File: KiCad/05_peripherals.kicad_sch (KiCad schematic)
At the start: 37 parts, among them IC501 VEML7700-TT, IC502 DS3231MZ+TRL, U502 DS18B20, U503 LM35-LP, U504 DHT11

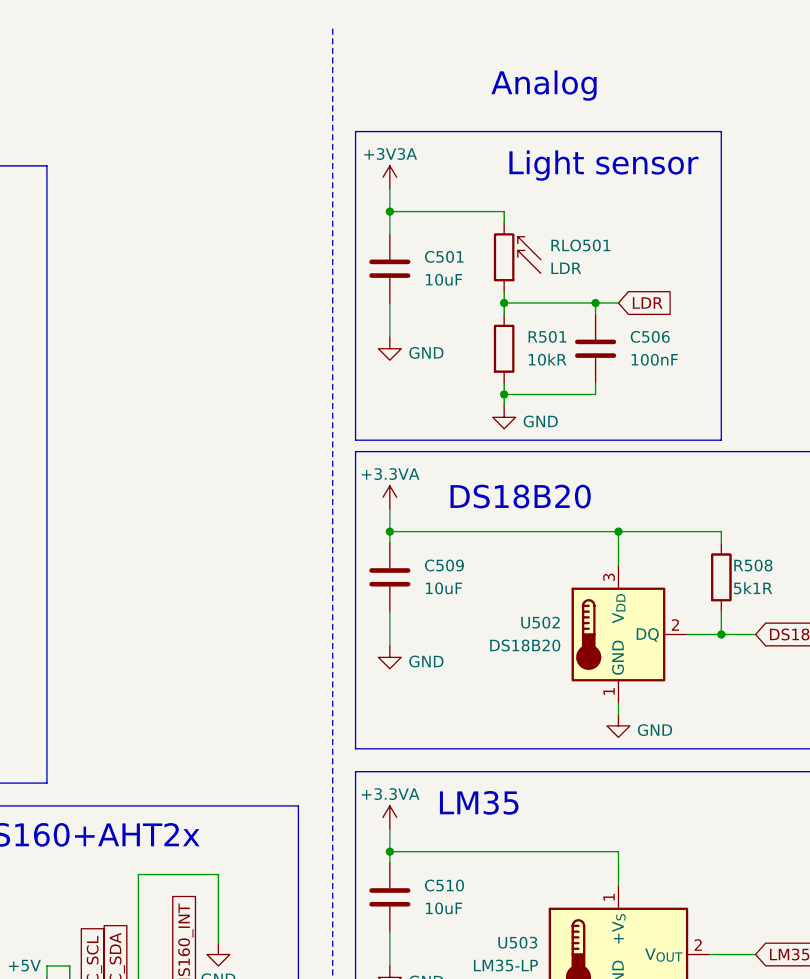
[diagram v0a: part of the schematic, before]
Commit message: Remove 3V3A power chain
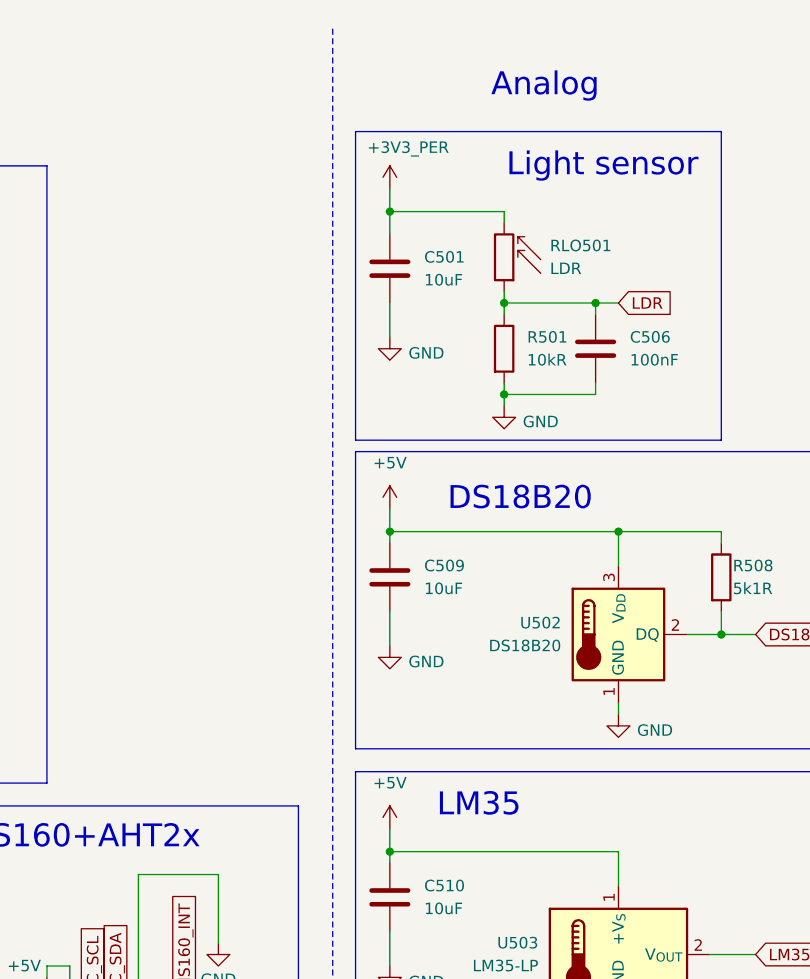
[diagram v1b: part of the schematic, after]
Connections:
- net +3.3VA is gone; now on net +5V: C509.1, C510.1, R508.1, U502.3 (V_{DD}), U503.1 (+V_{S})
- net +3V3A is gone; now on net +3V3_PER: C501.1, RLO501.2
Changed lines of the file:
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@@
 	)
 	(symbol
-		(lib_name "+3.3VA_1")
-		(lib_id "power:+3.3VA")
-		(at 224.79 104.14 0)
-		(unit 1)
-		(exclude_from_sim no)
-		(in_bom yes)
-		(on_board yes)
-		(dnp no)
-		(property "Reference" "#PWR0519"
-			(at 224.79 107.95 0)
-			(effects
-				(font
-					(size 1.27 1.27)
-				)
-				(hide yes)
-			)
-		)
-		(property "Value" "+3.3VA"
-			(at 224.79 100.33 0)
-			(effects
-				(font
-					(size 1.27 1.27)
-				)
-			)
-		)
-		(property "Footprint" ""
-			(at 224.79 104.14 0)
-			(effects
-				(font
-					(size 1.27 1.27)
-				)
-				(hide yes)
-			)
-		)
-		(property "Datasheet" ""
-			(at 224.79 104.14 0)
-			(effects
-				(font
-					(size 1.27 1.27)
-				)
-				(hide yes)
-			)
-		)
-		(property "Description" "Power symbol creates a global label with name \"+3.3VA\""
-			(at 224.79 104.14 0)
-			(effects
-				(font
-					(size 1.27 1.27)
-				)
-				(hide yes)
-			)
-		)
-		(pin "1"
-		)
-		(instances
-			(project "esp32_s3_weather_webserver"
-				(path "/04e96486-ec4c-4881-a0bf-37cb6ce91c2d/c3c48617-55df-481a-bcdd-56b688125780"
-					(reference "#PWR0519")
-					(unit 1)
-				)
-			)
-		)
-	)
-	(symbol
 		(lib_id "Device:C")
 		(at 62.23 116.84 0)
@@
 	)
 	(symbol
-		(lib_id "power:+3.3VA")
-		(at 224.79 33.02 0)
-		(unit 1)
-		(exclude_from_sim no)
-		(in_bom yes)
-		(on_board yes)
-		(dnp no)
-		(property "Reference" "#PWR0501"
-			(at 224.79 36.83 0)
-			(effects
-				(font
-					(size 1.27 1.27)
-				)
-				(hide yes)
-			)
-		)
-		(property "Value" "+3V3A"
-			(at 224.79 29.21 0)
-			(effects
-				(font
-					(size 1.27 1.27)
-				)
-			)
-		)
-		(property "Footprint" ""
-			(at 224.79 33.02 0)
-			(effects
-				(font
-					(size 1.27 1.27)
-				)
-				(hide yes)
-			)
-		)
-		(property "Datasheet" ""
-			(at 224.79 33.02 0)
-			(effects
-				(font
-					(size 1.27 1.27)
-				)
-				(hide yes)
-			)
-		)
-		(property "Description" "Power symbol creates a global label with name \"+3.3VA\""
-			(at 224.79 33.02 0)
-			(effects
-				(font
-					(size 1.27 1.27)
-				)
-				(hide yes)
-			)
-		)
-		(pin "1"
-		)
-		(instances
-			(project "esp32_s3_weather_webserver"
-				(path "/04e96486-ec4c-4881-a0bf-37cb6ce91c2d/c3c48617-55df-481a-bcdd-56b688125780"
-					(reference "#PWR0501")
-					(unit 1)
-				)
-			)
-		)
-	)
-	(symbol
 		(lib_id "esp32_s3_weather_webserver:SW_PUSH_6mm_H5mm")
 		(at 106.68 175.26 0)
@@
 	)
 	(symbol
+		(lib_id "power:+5V")
+		(at 224.79 104.14 0)
+		(mirror y)
+		(unit 1)
+		(exclude_from_sim no)
+		(in_bom yes)
+		(on_board yes)
+		(dnp no)
+		(fields_autoplaced yes)
+		(property "Reference" "#PWR014"
+			(at 224.79 107.95 0)
+			(effects
+				(font
+					(size 1.27 1.27)
+				)
+				(hide yes)
+			)
+		)
+		(property "Value" "+5V"
+			(at 224.79 99.06 0)
+			(effects
+				(font
+					(size 1.27 1.27)
+				)
+			)
+		)
+		(property "Footprint" ""
+			(at 224.79 104.14 0)
+			(effects
+				(font
+					(size 1.27 1.27)
+				)
+				(hide yes)
+			)
+		)
+		(property "Datasheet" ""
+			(at 224.79 104.14 0)
+			(effects
+				(font
+					(size 1.27 1.27)
+				)
+				(hide yes)
+			)
+		)
+		(property "Description" "Power symbol creates a global label with name \"+5V\""
+			(at 224.79 104.14 0)
+			(effects
+				(font
+					(size 1.27 1.27)
+				)
+				(hide yes)
+			)
+		)
+		(pin "1"
+		)
+		(instances
+			(project "esp32_s3_weather_webserver"
+				(path "/04e96486-ec4c-4881-a0bf-37cb6ce91c2d/c3c48617-55df-481a-bcdd-56b688125780"
+					(reference "#PWR014")
+					(unit 1)
+				)
+			)
+		)
+	)
+	(symbol
 		(lib_id "Device:C")
 		(at 134.62 119.38 0)
@@
 	)
 	(symbol
+		(lib_id "power:+5V")
+		(at 224.79 68.58 0)
+		(mirror y)
+		(unit 1)
+		(exclude_from_sim no)
+		(in_bom yes)
+		(on_board yes)
+		(dnp no)
+		(fields_autoplaced yes)
+		(property "Reference" "#PWR015"
+			(at 224.79 72.39 0)
+			(effects
+				(font
+					(size 1.27 1.27)
+				)
+				(hide yes)
+			)
+		)
+		(property "Value" "+5V"
+			(at 224.79 63.5 0)
+			(effects
+				(font
+					(size 1.27 1.27)
+				)
+			)
+		)
+		(property "Footprint" ""
+			(at 224.79 68.58 0)
+			(effects
+				(font
+					(size 1.27 1.27)
+				)
+				(hide yes)
+			)
+		)
+		(property "Datasheet" ""
+			(at 224.79 68.58 0)
+			(effects
+				(font
+					(size 1.27 1.27)
+				)
+				(hide yes)
+			)
+		)
+		(property "Description" "Power symbol creates a global label with name \"+5V\""
+			(at 224.79 68.58 0)
+			(effects
+				(font
+					(size 1.27 1.27)
+				)
+				(hide yes)
+			)
+		)
+		(pin "1"
+		)
+		(instances
+			(project "esp32_s3_weather_webserver"
+				(path "/04e96486-ec4c-4881-a0bf-37cb6ce91c2d/c3c48617-55df-481a-bcdd-56b688125780"
+					(reference "#PWR015")
+					(unit 1)
+				)
+			)
+		)
+	)
+	(symbol
 		(lib_id "power:+3.3V")
 		(at 123.19 113.03 0)
@@
 	)
 	(symbol
-		(lib_name "+3.3VA_2")
-		(lib_id "power:+3.3VA")
-		(at 224.79 68.58 0)
-		(unit 1)
-		(exclude_from_sim no)
-		(in_bom yes)
-		(on_board yes)
-		(dnp no)
-		(property "Reference" "#PWR0512"
-			(at 224.79 72.39 0)
-			(effects
-				(font
-					(size 1.27 1.27)
-				)
-				(hide yes)
-			)
-		)
-		(property "Value" "+3.3VA"
-			(at 224.79 64.77 0)
-			(effects
-				(font
-					(size 1.27 1.27)
-				)
-			)
-		)
-		(property "Footprint" ""
-			(at 224.79 68.58 0)
-			(effects
-				(font
-					(size 1.27 1.27)
-				)
-				(hide yes)
-			)
-		)
-		(property "Datasheet" ""
-			(at 224.79 68.58 0)
-			(effects
-				(font
-					(size 1.27 1.27)
-				)
-				(hide yes)
-			)
-		)
-		(property "Description" "Power symbol creates a global label with name \"+3.3VA\""
-			(at 224.79 68.58 0)
-			(effects
-				(font
-					(size 1.27 1.27)
-				)
-				(hide yes)
-			)
-		)
-		(pin "1"
-		)
-		(instances
-			(project "esp32_s3_weather_webserver"
-				(path "/04e96486-ec4c-4881-a0bf-37cb6ce91c2d/c3c48617-55df-481a-bcdd-56b688125780"
-					(reference "#PWR0512")
-					(unit 1)
-				)
-			)
-		)
-	)
-	(symbol
 		(lib_id "Device:C")
 		(at 50.8 116.84 0)
@@
 					(unit 1)
 				)
+			)
+		)
+	)
+	(symbol
+		(lib_id "power:+3.3V")
+		(at 224.79 33.02 0)
+		(unit 1)
+		(exclude_from_sim no)
+		(in_bom yes)
+		(on_board yes)
+		(dnp no)
+		(property "Reference" "#PWR016"
+			(at 224.79 36.83 0)
+			(effects
+				(font
+					(size 1.27 1.27)
+				)
+				(hide yes)
+			)
+		)
+		(property "Value" "+3V3_PER"
+			(at 226.822 28.448 0)
+			(effects
+				(font
+					(size 1.27 1.27)
+				)
+			)
+		)
+		(property "Footprint" ""
+			(at 224.79 33.02 0)
+			(effects
+				(font
+					(size 1.27 1.27)
+				)
+				(hide yes)
+			)
+		)
+		(property "Datasheet" ""
+			(at 224.79 33.02 0)
+			(effects
+				(font
+					(size 1.27 1.27)
+				)
+				(hide yes)
+			)
+		)
+		(property "Description" "Power symbol creates a global label with name \"+3.3V\""
+			(at 224.79 33.02 0)
+			(effects
+				(font
+					(size 1.27 1.27)
+				)
+				(hide yes)
+			)
+		)
+		(pin "1"
+		)
+		(instances
+			(project "esp32_s3_weather_webserver"
+				(path "/04e96486-ec4c-4881-a0bf-37cb6ce91c2d/c3c48617-55df-481a-bcdd-56b688125780"
+					(reference "#PWR016")
+					(unit 1)
+				)

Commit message: Add sensor footprints
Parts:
- U1: footprint (none) -> esp32_s3_weather_webserver:BME280
- U505: footprint (none) -> esp32_s3_weather_webserver:ENS160+AHT2x
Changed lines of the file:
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@@
 			)
 		)
-		(property "Footprint" ""
+		(property "Footprint" "esp32_s3_weather_webserver:ENS160+AHT2x"
 			(at 182.88 129.54 0)
 			(effects
@@
 			)
 		)
-		(property "Footprint" ""
+		(property "Footprint" "esp32_s3_weather_webserver:BME280"
 			(at 60.96 77.47 0)
 			(effects

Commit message: BOM updates
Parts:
- C501, C509, C510: footprint Capacitor_SMD:C_0805_2012Metric -> Capacitor_SMD:C_0603_1608Metric; Manufacturer Part Number CL21A106KOQNNNE -> CL10A106KP8NNNC
- IC501: Manufacturer (none) -> VISHAY; Manufacturer Part Number (none) -> VEML7700-TT
- IC502: Manufacturer (none) -> MAXIM; Manufacturer Part Number (none) -> DS3231MZ+TRL; now not fitted
- R508, R509: footprint Resistor_SMD:R_0402_1005Metric -> Resistor_SMD:R_0805_2012Metric; Manufacturer Part Number 0402WGF5101TCE -> 0805W8F5101T5E
- SW1, SW2, SW403: Manufacturer (none) -> SM Switch; Manufacturer Part Number (none) -> SMG-01-H080A1
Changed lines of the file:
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@@
 			)
 		)
+		(property "Manufacturer" "SM Switch"
+			(at 25.4 175.26 0)
+			(effects
+				(font
+					(size 1.27 1.27)
+				)
+				(hide yes)
+			)
+		)
+		(property "Manufacturer Part Number" "SMG-01-H080A1"
+			(at 25.4 175.26 0)
+			(effects
+				(font
+					(size 1.27 1.27)
+				)
+				(hide yes)
+			)
+		)
 		(pin "2"
 		)
@@
 			)
 		)
+		(property "Manufacturer" "VISHAY"
+			(at 160.02 64.77 0)
+			(effects
+				(font
+					(size 1.27 1.27)
+				)
+				(hide yes)
+			)
+		)
+		(property "Manufacturer Part Number" "VEML7700-TT"
+			(at 160.02 64.77 0)
+			(effects
+				(font
+					(size 1.27 1.27)
+				)
+				(hide yes)
+			)
+		)
 		(pin "2"
 		)
@@
 			)
 		)
+		(property "Manufacturer" "SM Switch"
+			(at 106.68 175.26 0)
+			(effects
+				(font
+					(size 1.27 1.27)
+				)
+				(hide yes)
+			)
+		)
+		(property "Manufacturer Part Number" "SMG-01-H080A1"
+			(at 106.68 175.26 0)
+			(effects
+				(font
+					(size 1.27 1.27)
+				)
+				(hide yes)
+			)
+		)
 		(pin "2"
 		)
@@
 			)
 		)
-		(property "Footprint" "Capacitor_SMD:C_0805_2012Metric"
+		(property "Footprint" "Capacitor_SMD:C_0603_1608Metric"
 			(at 225.7552 115.57 0)
 			(effects
@@
 			)
 		)
-		(property "Manufacturer Part Number" "CL21A106KOQNNNE"
+		(property "Manufacturer Part Number" "CL10A106KP8NNNC"
 			(at 224.79 111.76 0)
 			(effects
@@
 			)
 		)
-		(property "Footprint" "Capacitor_SMD:C_0805_2012Metric"
+		(property "Footprint" "Capacitor_SMD:C_0603_1608Metric"
 			(at 225.7552 80.01 0)
 			(effects
@@
 			)
 		)
-		(property "Manufacturer Part Number" "CL21A106KOQNNNE"
+		(property "Manufacturer Part Number" "CL10A106KP8NNNC"
 			(at 224.79 76.2 0)
 			(effects
@@
 			)
 		)
+		(property "Manufacturer" "SM Switch"
+			(at 63.5 175.26 0)
+			(effects
+				(font
+					(size 1.27 1.27)
+				)
+				(hide yes)
+			)
+		)
+		(property "Manufacturer Part Number" "SMG-01-H080A1"
+			(at 63.5 175.26 0)
+			(effects
+				(font
+					(size 1.27 1.27)
+				)
+				(hide yes)
+			)
+		)
 		(pin "2"
 		)
@@
 			)
 		)
-		(property "Footprint" "Capacitor_SMD:C_0805_2012Metric"
+		(property "Footprint" "Capacitor_SMD:C_0603_1608Metric"
 			(at 225.7552 45.72 0)
 			(effects
@@
 			)
 		)
-		(property "Manufacturer Part Number" "CL21A106KOQNNNE"
+		(property "Manufacturer Part Number" "CL10A106KP8NNNC"
 			(at 224.79 41.91 0)
 			(effects
@@
 		(in_bom yes)
 		(on_board yes)
-		(dnp no)
+		(dnp yes)
 		(fields_autoplaced yes)
 		(property "Reference" "IC502"
@@
 			)
 		)
+		(property "Manufacturer" "MAXIM"
+			(at 60.96 127 0)
+			(effects
+				(font
+					(size 1.27 1.27)
+				)
+				(hide yes)
+			)
+		)
+		(property "Manufacturer Part Number" "DS3231MZ+TRL"
+			(at 60.96 127 0)
+			(effects
+				(font
+					(size 1.27 1.27)
+				)
+				(hide yes)
+			)
+		)
 		(pin "5"
 		)
@@
 			)
 		)
-		(property "Footprint" "Resistor_SMD:R_0402_1005Metric"
+		(property "Footprint" "Resistor_SMD:R_0805_2012Metric"
 			(at 259.842 76.2 90)
 			(effects
@@
 			)
 		)
-		(property "Manufacturer Part Number" "0402WGF5101TCE"
+		(property "Manufacturer Part Number" "0805W8F5101T5E"
 			(at 261.62 76.2 0)
 			(effects
@@
 			)
 		)
-		(property "Footprint" "Resistor_SMD:R_0402_1005Metric"
+		(property "Footprint" "Resistor_SMD:R_0805_2012Metric"
 			(at 121.412 119.38 90)
 			(effects
@@
 			)
 		)
-		(property "Manufacturer Part Number" "0402WGF5101TCE"
+		(property "Manufacturer Part Number" "0805W8F5101T5E"
 			(at 123.19 119.38 0)
 			(effects

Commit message: BOM updates. First layout
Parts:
- removed C502: 10uF, Capacitor_SMD:C_0603_1608Metric, symbol Device:C
- removed C503: 100nF, Capacitor_SMD:C_0603_1608Metric, symbol Device:C
- C502: renamed from C506; footprint Capacitor_SMD:C_0603_1608Metric -> Capacitor_SMD:C_0402_1005Metric; Manufacturer Part Number CL10B104KB8NNNC -> CL05B104KO5NNNC
- C504: renamed from C508; footprint Capacitor_SMD:C_0603_1608Metric -> Capacitor_SMD:C_0402_1005Metric; Manufacturer Part Number CL10B104KB8NNNC -> CL05B104KO5NNNC
- C508: renamed from C512; footprint Capacitor_SMD:C_0603_1608Metric -> Capacitor_SMD:C_0402_1005Metric; Manufacturer Part Number CL10B104KB8NNNC -> CL05B104KO5NNNC
- C510: renamed from C514; footprint Capacitor_SMD:C_0603_1608Metric -> Capacitor_SMD:C_0402_1005Metric; Manufacturer Part Number CL10B104KB8NNNC -> CL05B104KO5NNNC
- C511: renamed from C409; footprint Capacitor_SMD:C_0603_1608Metric -> Capacitor_SMD:C_0402_1005Metric; Manufacturer Part Number CL10B104KB8NNNC -> CL05B104KO5NNNC
- C512: renamed from C1; footprint Capacitor_SMD:C_0603_1608Metric -> Capacitor_SMD:C_0402_1005Metric; Manufacturer Part Number CL10B104KB8NNNC -> CL05B104KO5NNNC
- C513: renamed from C2; footprint Capacitor_SMD:C_0603_1608Metric -> Capacitor_SMD:C_0402_1005Metric; Manufacturer Part Number CL10B104KB8NNNC -> CL05B104KO5NNNC
- IC502: now fitted
- R501, R502, R503: footprint Resistor_SMD:R_0805_2012Metric -> Resistor_SMD:R_0402_1005Metric
- R504: renamed from R508; footprint Resistor_SMD:R_0805_2012Metric -> Resistor_SMD:R_0402_1005Metric; Manufacturer Part Number 0805W8F5101T5E -> 0402WGF5101TCE
- R505: renamed from R509; footprint Resistor_SMD:R_0805_2012Metric -> Resistor_SMD:R_0402_1005Metric; Manufacturer Part Number 0805W8F5101T5E -> 0402WGF5101TCE
- R506: renamed from R510; footprint Resistor_SMD:R_0805_2012Metric -> Resistor_SMD:R_0402_1005Metric
- R507: renamed from R511; footprint Resistor_SMD:R_0805_2012Metric -> Resistor_SMD:R_0402_1005Metric
- R508: renamed from R409; footprint Resistor_SMD:R_0805_2012Metric -> Resistor_SMD:R_0402_1005Metric
- R509: renamed from R1; footprint Resistor_SMD:R_0805_2012Metric -> Resistor_SMD:R_0402_1005Metric
- R510: renamed from R2; footprint Resistor_SMD:R_0805_2012Metric -> Resistor_SMD:R_0402_1005Metric
- renumbered C507 to C503, C509 to C505, C510 to C506, C511 to C507, C513 to C509, SW403 to SW501, SW1 to SW502, SW2 to SW503, U1 to U501
